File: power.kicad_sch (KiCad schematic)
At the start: 128 parts, among them Q2 BC817-25W, Q3 DZDH0401DW, Q4 DZDH0401DW, Q5 SI7613DN-T1-GE3, Q6 SI7613DN-T1-GE3, U1 LT8350RV#PBF, U2 MP2386GG, U3 TPS65983BAZBHR

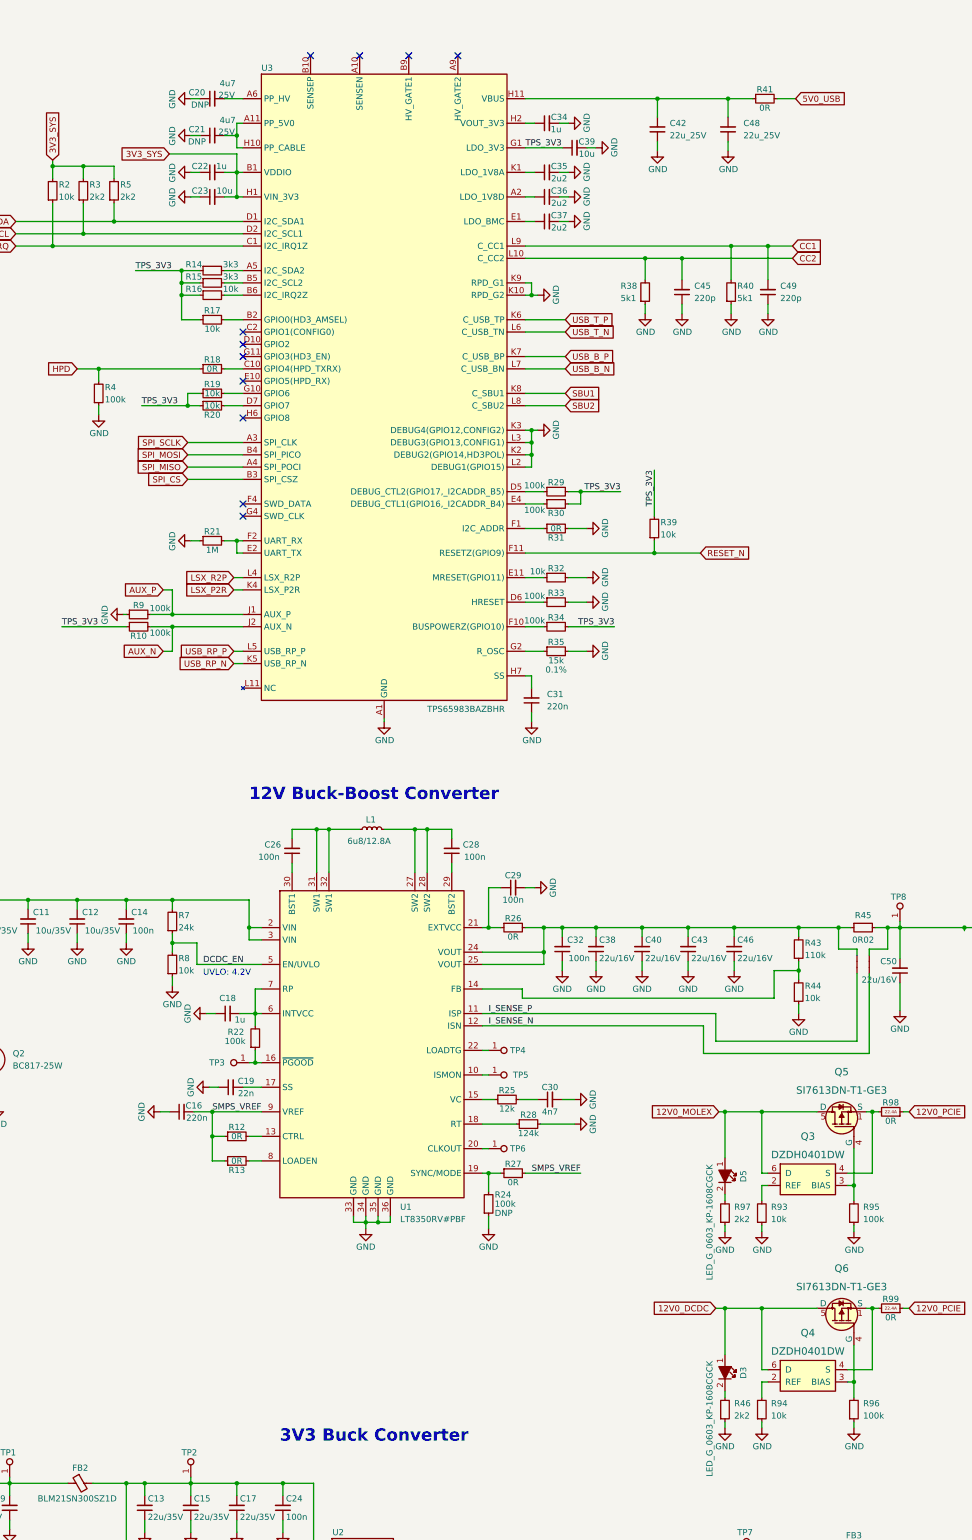
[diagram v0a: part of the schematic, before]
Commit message: Update all symbols from library to fix issues shown by klibs-check-license script
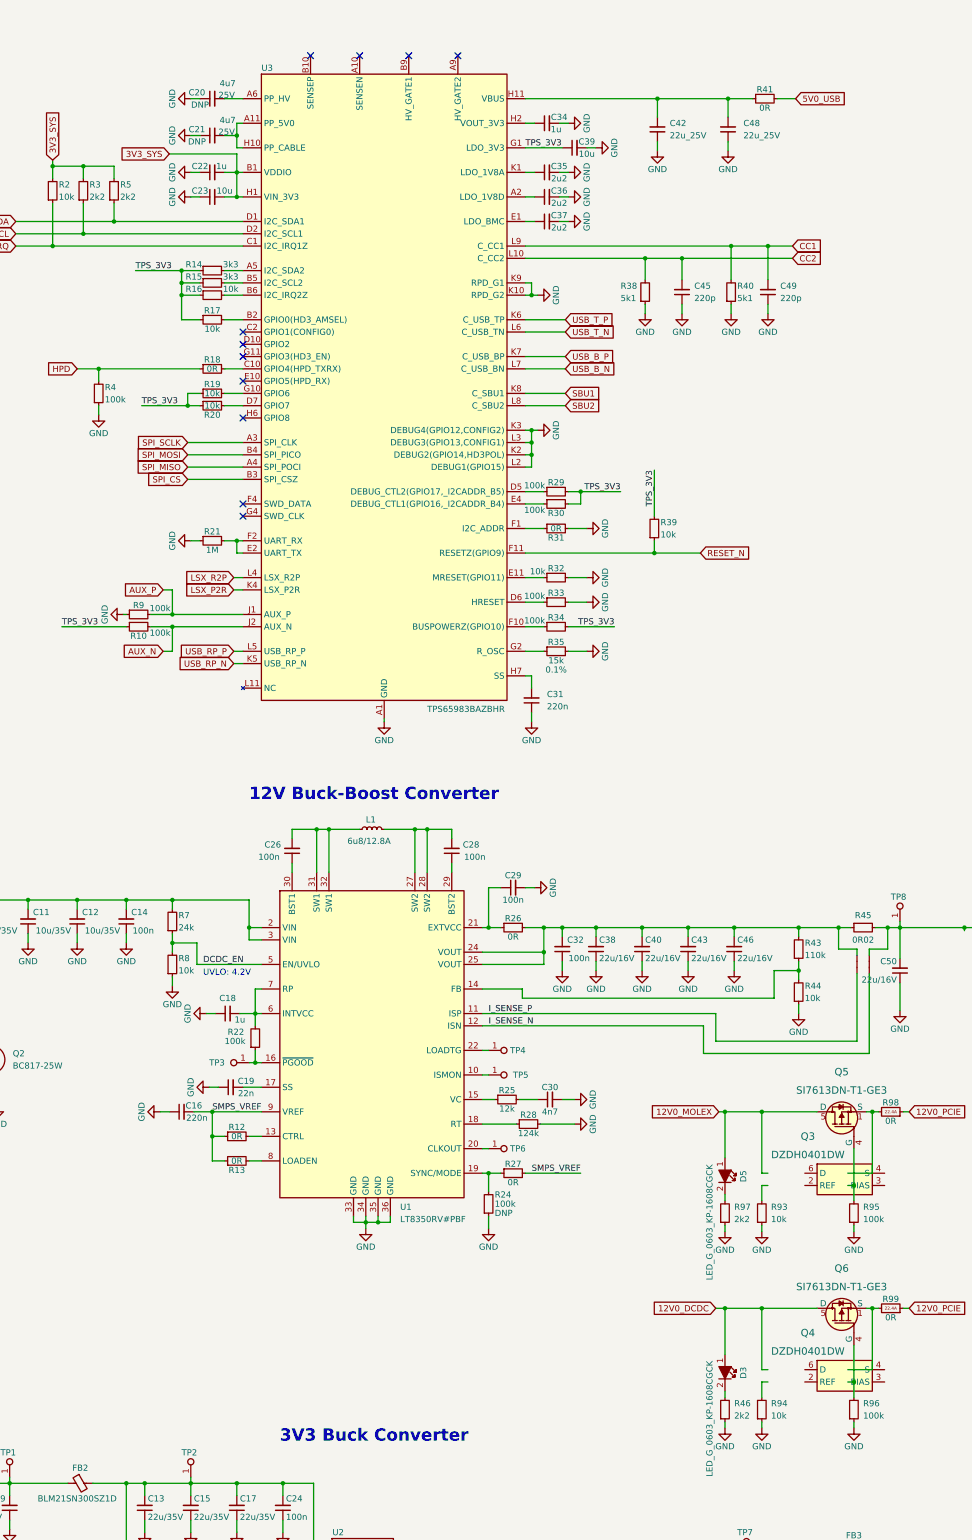
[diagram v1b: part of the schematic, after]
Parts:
- C10, C11, C119, C12, C122, C13, C14, C15, C16, C17, C18, C19, C20, C21, C22, C23, C24, C25, C26, C27, C28, C29, C30, C31, C32, C33, C34, C35, C36, C37, C38, C39, C40, C41, C42, C43, C44, C45, C46, C47, C48, C49, C50, C7, C8, C9, D1, D2, D3, D5, FB1, FB2, FB3, L1, L2, Q2, R10, R11, R12, R13, R14, R15, R16, R17, R18, R19, R2, R20, R21, R22, R23, R24, R25, R26, R27, R29, R3, R30, R31, R32, R33, R34, R35, R36, R37, R38, R39, R4, R40, R41, R42, R43, R44, R45, R46, R5, R6, R7, R8, R9, R91, R92, R97, U1, U2, U3: Author (none) -> Antmicro; Copyright Copyright (c) 2023 Antmicro -> (none); License Apache-2.0 License -> Apache-2.0
- Q3, Q4: Author (none) -> Antmicro; License (none) -> Apache-2.0; MPN DZDH0401DW -> DZDH0401DW-7
- TP1, TP12, TP2, TP3, TP5, TP7, TP8: footprint antmicro-footprints:TP_SMD_1mm -> antmicro-footprints:Testpoint_smd_1mm; Author (none) -> Antmicro; Copyright Copyright (c) 2023 Antmicro -> (none); License Apache-2.0 License -> Apache-2.0; Manufacturer None -> (none)
- TP4, TP6: Author (none) -> Antmicro; Copyright Copyright (c) 2023 Antmicro -> (none); License Apache-2.0 License -> Apache-2.0; Manufacturer None -> (none)
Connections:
- net 12V0_DCDC: no longer Q4.6 (D)
- net 12V0_MOLEX: no longer Q3.6 (D)
- net at Q6.1 (S), Q6.2 (S), Q6.3 (S)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: no longer Q4.4 (S)
- net at Q3.2 (REF): no longer R93.2
- net at Q5.4 (G), R95.2: no longer Q3.3 (BIAS)
- net at Q5.1 (S), Q5.2 (S), Q5.3 (S)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: no longer Q3.4 (S)
- net at Q6.4 (G), R96.2: no longer Q4.3 (BIAS)
- net at R94.2: no longer Q4.2 (REF)
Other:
- moved on the sheet: Q3, Q4

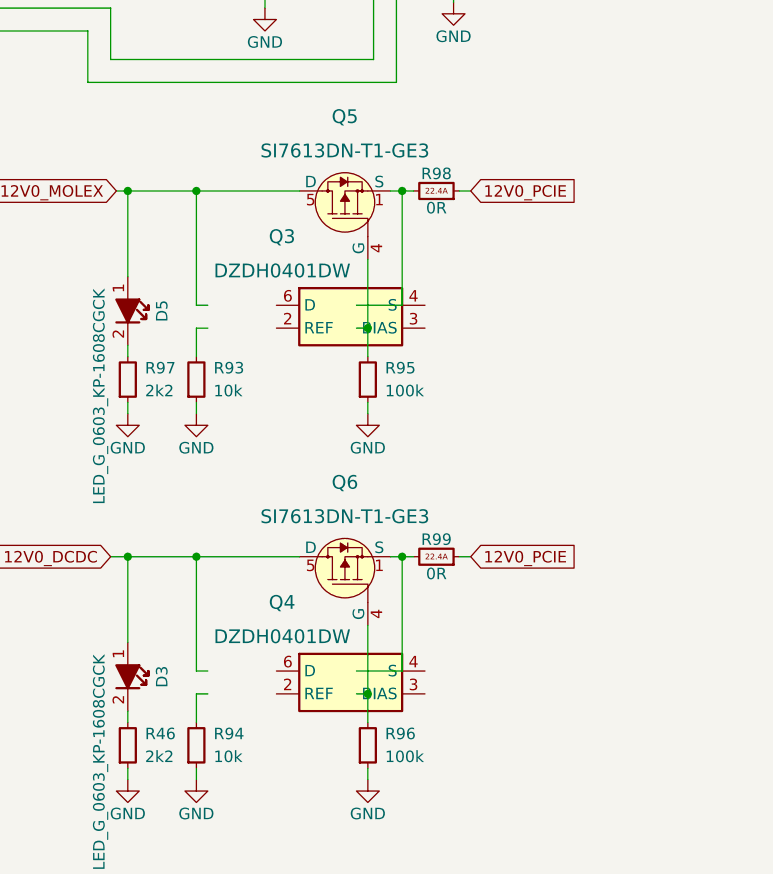
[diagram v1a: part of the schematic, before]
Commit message: Standardize and update SI7613DN-T1-GE3 symbol, fix spotted issues on symbols placement
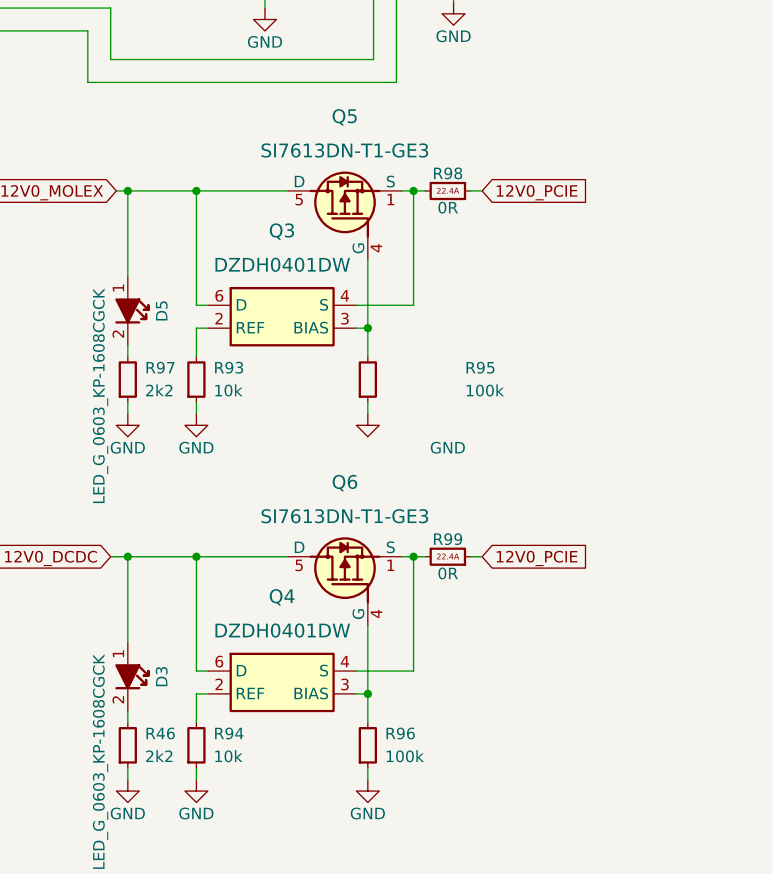
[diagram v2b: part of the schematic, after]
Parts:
- Q5, Q6: Author (none) -> Antmicro; License (none) -> Apache-2.0
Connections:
- net 12V0_DCDC: now also Q4.6 (D)
- net 12V0_MOLEX: now also Q3.6 (D)
- net at Q6.1 (S), Q6.2 (S), Q6.3 (S)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: now also Q4.4 (S)
- net at Q3.2 (REF): now also R93.2
- net at Q3.3 (BIAS): now also Q5.4 (G), R95.2
- net at Q3.4 (S): now also Q5.1 (S), Q5.2 (S), Q5.3 (S), R98.2
- net at Q6.4 (G), R96.2: now also Q4.3 (BIAS)
- net at R94.2: now also Q4.2 (REF)
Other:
- moved on the sheet: Q3, Q4, R98, R99

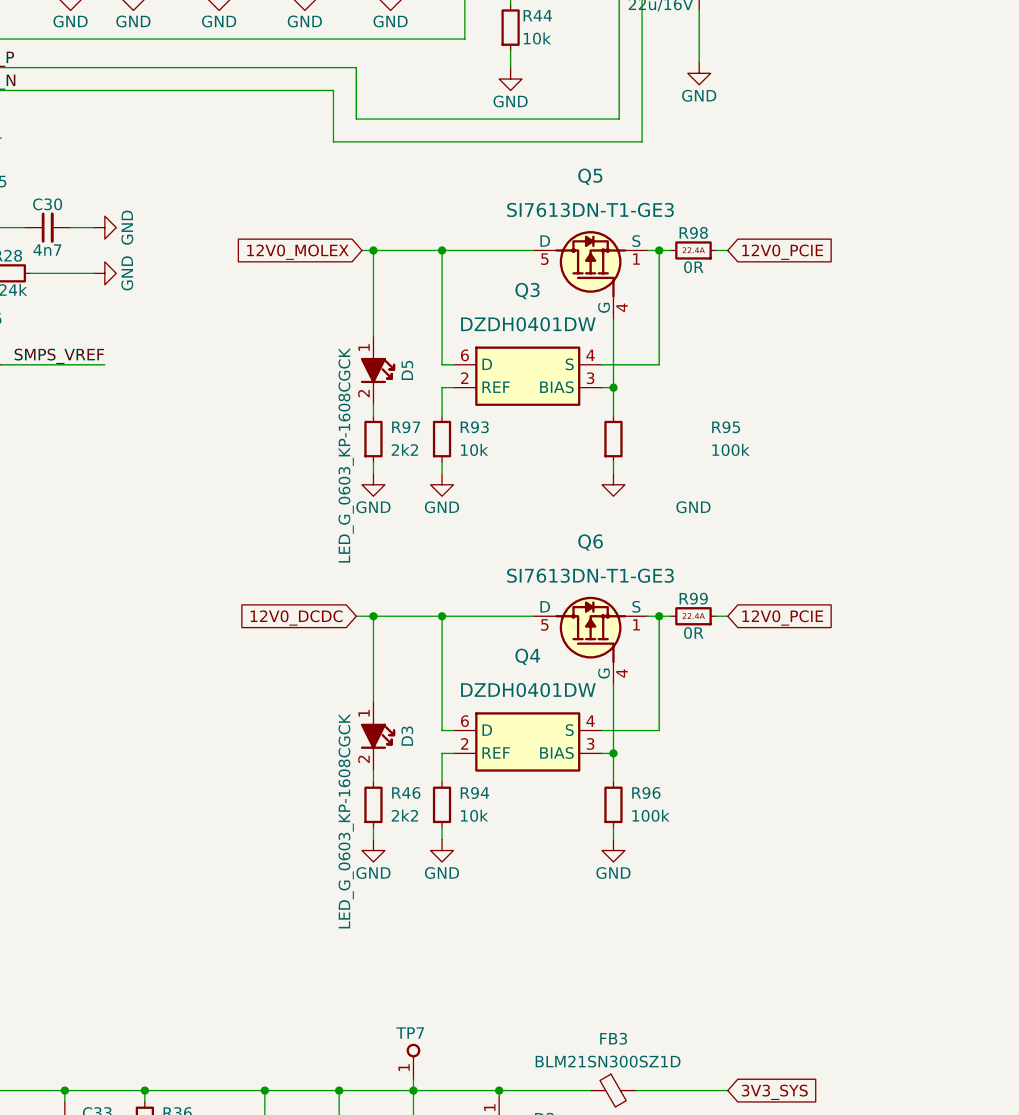
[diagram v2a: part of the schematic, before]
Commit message: Standardize all symbols on schematic
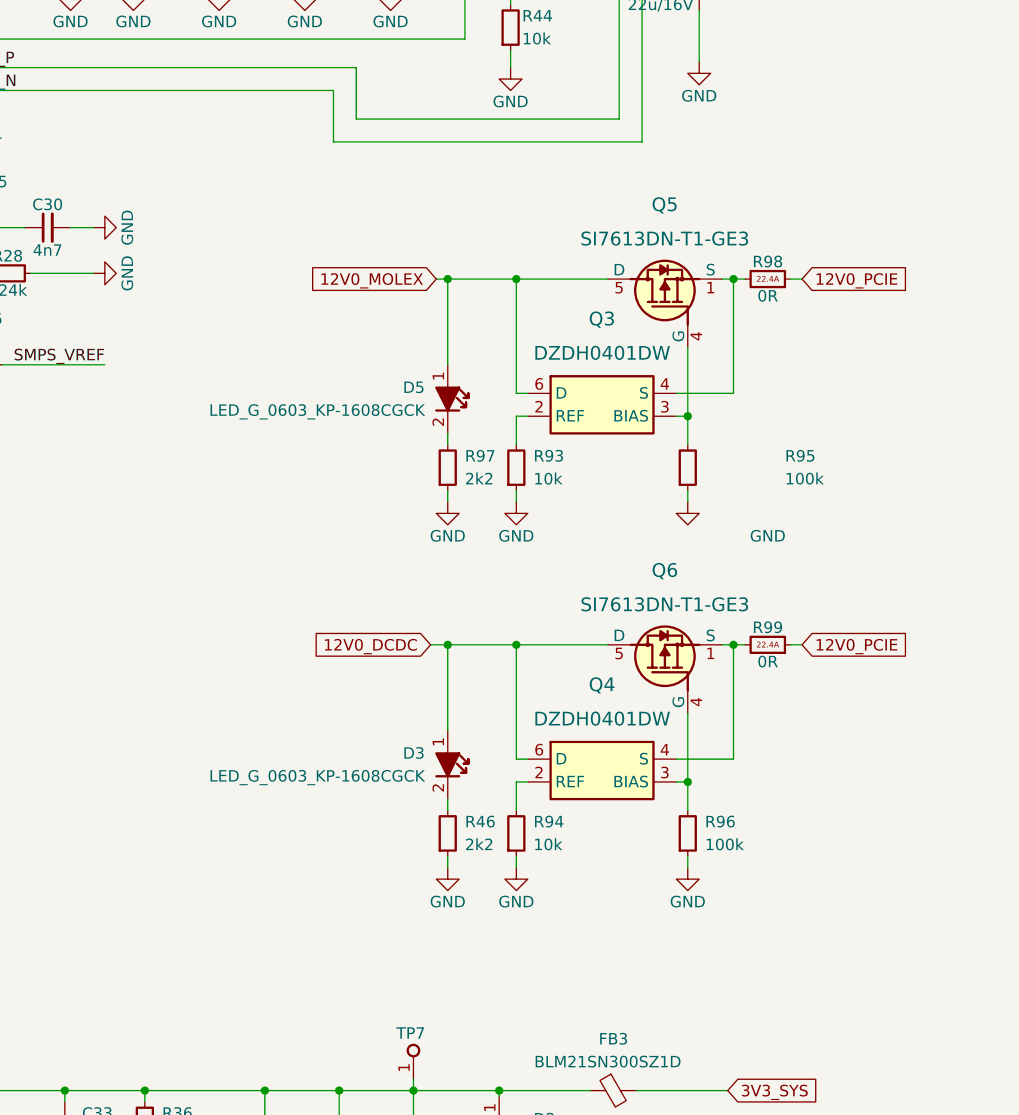
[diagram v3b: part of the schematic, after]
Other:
- moved on the sheet: D3, D5, Q3, Q4, Q5, Q6, R46, R93, R94, R95, R96, R97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

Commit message: Update naming convention
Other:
- title: (none) -> Thunderbolt PCIe Adaper
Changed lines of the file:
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@@
   (paper "A3" portrait)
   (title_block
-    (date "2023-05-09")
+    (title "Thunderbolt PCIe Adaper")
+    (date "2023-06-05")
     (rev "1.0.0")
     (comment 1 "www.antmicro.com")

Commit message: Change symbol of U4, redraw schematic to use landscape orientation
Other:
- note added: "Ideal diodes"
- moved on the sheet: C10, C11, C119, C12, C122, C13, C14, C15, C16, C17, C18, C19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

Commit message: Generate library of local components
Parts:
- C10, C13, C15, C17, C8: footprint antmicro-footprints:C_1206_3216Metric -> thunderbolt-pcie-adapter-footprints:C_1206_3216Metric; symbol antmicroCapacitorsmisc:C_22u_1206_35V -> thunderbolt-pcie-adapter:C_22u_1206_35V
- C11, C12, C7, C9: footprint antmicro-footprints:C_0805_2012Metric -> thunderbolt-pcie-adapter-footprints:C_0805_2012Metric; symbol antmicroCapacitorsmisc:C_10u_0805_35V -> thunderbolt-pcie-adapter:C_10u_0805_35V
- C119, C122, C38, C40, C43, C46, C50: footprint antmicro-footprints:C_0603_1608Metric -> thunderbolt-pcie-adapter-footprints:C_0603_1608Metric; symbol antmicroCapacitors0603:C_22u_16V_0603 -> thunderbolt-pcie-adapter:C_22u_16V_0603
- C14, C24, C26, C28, C29, C32: footprint antmicro-footprints:C_0402_1005Metric -> thunderbolt-pcie-adapter-footprints:C_0402_1005Metric; symbol antmicroCapacitors0402:C_100n_0402 -> thunderbolt-pcie-adapter:C_100n_0402
- C16, C27, C31: footprint antmicro-footprints:C_0402_1005Metric -> thunderbolt-pcie-adapter-footprints:C_0402_1005Metric; symbol antmicroCapacitors0402:C_220n_0402 -> thunderbolt-pcie-adapter:C_220n_0402
- C18, C22, C25, C34: footprint antmicro-footprints:C_0402_1005Metric -> thunderbolt-pcie-adapter-footprints:C_0402_1005Metric; symbol antmicroCapacitors0402:C_1u_0402 -> thunderbolt-pcie-adapter:C_1u_0402
- C19: footprint antmicro-footprints:C_0402_1005Metric -> thunderbolt-pcie-adapter-footprints:C_0402_1005Metric; symbol antmicroCapacitors0402:C_22n_0402 -> thunderbolt-pcie-adapter:C_22n_0402
- C20, C21: footprint antmicro-footprints:C_0402_1005Metric -> thunderbolt-pcie-adapter-footprints:C_0402_1005Metric; symbol antmicroCapacitors0402:C_4u7_25V_0402 -> thunderbolt-pcie-adapter:C_4u7_25V_0402
- C23, C39: footprint antmicro-footprints:C_0402_1005Metric -> thunderbolt-pcie-adapter-footprints:C_0402_1005Metric; symbol antmicroCapacitors0402:C_10u_0402 -> thunderbolt-pcie-adapter:C_10u_0402
- C30: footprint antmicro-footprints:C_0402_1005Metric -> thunderbolt-pcie-adapter-footprints:C_0402_1005Metric; symbol antmicroCapacitors0402:C_4n7_0402 -> thunderbolt-pcie-adapter:C_4n7_0402
- C33: footprint antmicro-footprints:C_0402_1005Metric -> thunderbolt-pcie-adapter-footprints:C_0402_1005Metric; symbol antmicroCapacitors0402:C_33p_0402 -> thunderbolt-pcie-adapter:C_33p_0402
- C35, C36, C37: footprint antmicro-footprints:C_0402_1005Metric -> thunderbolt-pcie-adapter-footprints:C_0402_1005Metric; symbol antmicroCapacitors0402:C_2u2_0402 -> thunderbolt-pcie-adapter:C_2u2_0402
- C41, C44, C47: footprint antmicro-footprints:C_0603_1608Metric -> thunderbolt-pcie-adapter-footprints:C_0603_1608Metric; symbol antmicroCapacitors0603:C_22u_0603 -> thunderbolt-pcie-adapter:C_22u_0603
- C42, C48: footprint antmicro-footprints:C_0805_2012Metric -> thunderbolt-pcie-adapter-footprints:C_0805_2012Metric; symbol antmicroCapacitorsmisc:C_22u_25V_0805 -> thunderbolt-pcie-adapter:C_22u_25V_0805
- C45, C49: footprint antmicro-footprints:C_0402_1005Metric -> thunderbolt-pcie-adapter-footprints:C_0402_1005Metric; symbol antmicroCapacitors0402:C_220p_0402 -> thunderbolt-pcie-adapter:C_220p_0402
- D1: footprint antmicro-footprints:D_SOD-323F -> thunderbolt-pcie-adapter-footprints:D_SOD-323F; symbol antmicroDiodesZenerSingle:MM3Z3V3C -> thunderbolt-pcie-adapter:MM3Z3V3C
- D2, D3, D5: footprint antmicro-footprints:LED_0603_1608Metric_G -> thunderbolt-pcie-adapter-footprints:LED_0603_1608Metric_G; symbol antmicroLEDIndicationDiscrete:LED_G_0603_KP-1608CGCK -> thunderbolt-pcie-adapter:LED_G_0603_KP-1608CGCK
- FB1, FB2, FB3: footprint antmicro-footprints:FB_0805_2012Metric -> thunderbolt-pcie-adapter-footprints:FB_0805_2012Metric; symbol antmicroFerriteBeadsandChips:BLM21SN300SZ1D -> thunderbolt-pcie-adapter:BLM21SN300SZ1D
- L1: footprint antmicro-footprints:L_Coilcraft_XAL7070 -> thunderbolt-pcie-adapter-footprints:L_Coilcraft_XAL7070; symbol antmicroFixedInductors:L_6u8_12.8A_XAL7070 -> thunderbolt-pcie-adapter:L_6u8_12.8A_XAL7070
- L2: footprint antmicro-footprints:L_Coilcraft_XAL5030 -> thunderbolt-pcie-adapter-footprints:L_Coilcraft_XAL5030; symbol antmicroFixedInductors:L_2u2_10.4A_XAL5030 -> thunderbolt-pcie-adapter:L_2u2_10.4A_XAL5030
- Q2: footprint antmicro-footprints:SOT-323 -> thunderbolt-pcie-adapter-footprints:SOT-323; symbol antmicroTransistorsBipolarSingle:BC817-25W -> thunderbolt-pcie-adapter:BC817-25W
- Q3, Q4: footprint antmicro-footprints:SOT-363 -> thunderbolt-pcie-adapter-footprints:SOT-363; symbol antmicroPMICORControllersIdealDiodes:DZDH0401DW -> thunderbolt-pcie-adapter:DZDH0401DW
- Q5, Q6: footprint antmicro-footprints:Vishay_PowerPAK_1212-8_Single -> thunderbolt-pcie-adapter-footprints:Vishay_PowerPAK_1212-8_Single; symbol antmicroTransistorsFETsMOSFETsSingle:SI7613DN-T1-GE3 -> thunderbolt-pcie-adapter:SI7613DN-T1-GE3
- R10, R22, R23, R24, R29, R30, R33, R34, R4, R9, R92, R95, R96: footprint antmicro-footprints:R_0402_1005Metric -> thunderbolt-pcie-adapter-footprints:R_0402_1005Metric; symbol antmicroResistors0402:R_100k_0402 -> thunderbolt-pcie-adapter:R_100k_0402
- R11, R16, R17, R19, R2, R20, R32, R39, R44, R6, R8, R91, R93, R94: footprint antmicro-footprints:R_0402_1005Metric -> thunderbolt-pcie-adapter-footprints:R_0402_1005Metric; symbol antmicroResistors0402:R_10k_0402 -> thunderbolt-pcie-adapter:R_10k_0402
- R12, R13, R18, R26, R27, R31: footprint antmicro-footprints:R_0402_1005Metric -> thunderbolt-pcie-adapter-footprints:R_0402_1005Metric; symbol antmicroResistors0402:R_0R_0402 -> thunderbolt-pcie-adapter:R_0R_0402
- R14, R15: footprint antmicro-footprints:R_0402_1005Metric -> thunderbolt-pcie-adapter-footprints:R_0402_1005Metric; symbol antmicroResistors0402:R_3k3_0402 -> thunderbolt-pcie-adapter:R_3k3_0402
- R21: footprint antmicro-footprints:R_0402_1005Metric -> thunderbolt-pcie-adapter-footprints:R_0402_1005Metric; symbol antmicroResistors0402:R_1M_0402 -> thunderbolt-pcie-adapter:R_1M_0402
- R25: footprint antmicro-footprints:R_0402_1005Metric -> thunderbolt-pcie-adapter-footprints:R_0402_1005Metric; symbol antmicroResistors0402:R_12k_0402 -> thunderbolt-pcie-adapter:R_12k_0402
- R28: footprint antmicro-footprints:R_0402_1005Metric -> thunderbolt-pcie-adapter-footprints:R_0402_1005Metric; symbol antmicroResistors0402:R_124k_0402 -> thunderbolt-pcie-adapter:R_124k_0402
- R3, R46, R5, R97: footprint antmicro-footprints:R_0402_1005Metric -> thunderbolt-pcie-adapter-footprints:R_0402_1005Metric; symbol antmicroResistors0402:R_2k2_0402 -> thunderbolt-pcie-adapter:R_2k2_0402
- R35: footprint antmicro-footprints:R_0402_1005Metric -> thunderbolt-pcie-adapter-footprints:R_0402_1005Metric; symbol antmicroResistors0402:R_15k_0.1%_0402 -> thunderbolt-pcie-adapter:R_15k_0.1%_0402
- R36: footprint antmicro-footprints:R_0402_1005Metric -> thunderbolt-pcie-adapter-footprints:R_0402_1005Metric; symbol antmicroResistors0402:R_40k2_0402 -> thunderbolt-pcie-adapter:R_40k2_0402
- R37: footprint antmicro-footprints:R_0402_1005Metric -> thunderbolt-pcie-adapter-footprints:R_0402_1005Metric; symbol antmicroResistors0402:R_8k87_0402 -> thunderbolt-pcie-adapter:R_8k87_0402
- R38, R40: footprint antmicro-footprints:R_0402_1005Metric -> thunderbolt-pcie-adapter-footprints:R_0402_1005Metric; symbol antmicroResistors0402:R_5k1_0402 -> thunderbolt-pcie-adapter:R_5k1_0402
- R41: footprint antmicro-footprints:R_0603_1608Metric -> thunderbolt-pcie-adapter-footprints:R_0603_1608Metric; symbol antmicroResistors0603:R_0R_0603 -> thunderbolt-pcie-adapter:R_0R_0603
- R42: footprint antmicro-footprints:R_0402_1005Metric -> thunderbolt-pcie-adapter-footprints:R_0402_1005Metric; symbol antmicroResistors0402:R_330R_0402 -> thunderbolt-pcie-adapter:R_330R_0402
- R43: footprint antmicro-footprints:R_0402_1005Metric -> thunderbolt-pcie-adapter-footprints:R_0402_1005Metric; symbol antmicroResistors0402:R_110k_0402 -> thunderbolt-pcie-adapter:R_110k_0402
- R45: footprint antmicro-footprints:R_1206_3216Metric -> thunderbolt-pcie-adapter-footprints:R_1206_3216Metric; symbol antmicroResistorsmisc:R_0R02_1206 -> thunderbolt-pcie-adapter:R_0R02_1206
- R7: footprint antmicro-footprints:R_0402_1005Metric -> thunderbolt-pcie-adapter-footprints:R_0402_1005Metric; symbol antmicroResistors0402:R_24k_0402 -> thunderbolt-pcie-adapter:R_24k_0402
- R98, R99: footprint antmicro-footprints:R_0603_1608Metric -> thunderbolt-pcie-adapter-footprints:R_0603_1608Metric; symbol antmicroResistors0603:R_0R_22.4A_0603 -> thunderbolt-pcie-adapter:R_0R_22.4A_0603
- TP1, TP12, TP2, TP3, TP5, TP7, TP8: footprint antmicro-footprints:Testpoint_smd_1mm -> thunderbolt-pcie-adapter-footprints:Testpoint_smd_1mm; symbol antmicroTestPoints:TP_1mm_SMD -> thunderbolt-pcie-adapter:TP_1mm_SMD
- TP10, TP11: footprint antmicro-footprints:NetTie-2_SMD_Pad0.127mm -> thunderbolt-pcie-adapter-footprints:NetTie-2_SMD_Pad0.127mm; symbol antmicroShuntsJumpers:Net-Tie_2 -> thunderbolt-pcie-adapter:Net-Tie_2
- TP4, TP6: footprint antmicro-footprints:TP_SMD_0.75mm -> thunderbolt-pcie-adapter-footprints:TP_SMD_0.75mm; symbol antmicroTestPoints:TP_0.75mm_SMD -> thunderbolt-pcie-adapter:TP_0.75mm_SMD
- U1: footprint antmicro-footprints:LT8350 -> thunderbolt-pcie-adapter-footprints:LT8350; symbol antmicroDCDCConverters:LT8350RV#PBF -> thunderbolt-pcie-adapter:LT8350RV#PBF
- U2: footprint antmicro-footprints:QFN-11_2x2mm_P0.5mm -> thunderbolt-pcie-adapter-footprints:QFN-11_2x2mm_P0.5mm; symbol antmicroDCDCConverters:MP2386GG -> thunderbolt-pcie-adapter:MP2386GG
- U3: footprint antmicro-footprints:IC_TPS65983BAZBHR -> thunderbolt-pcie-adapter-footprints:IC_TPS65983BAZBHR; symbol antmicroInterfaceControllers:TPS65983BAZBHR -> thunderbolt-pcie-adapter:TPS65983BAZBHR
